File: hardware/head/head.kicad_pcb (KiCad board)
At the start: 2 copper layers, 80 x 55 mm, 50 parts, among them J1 Head bundle, J10 CM4 socket 101-200, J2 ToF, J3 I2C breakout, J4 Eye LED, J5 Speaker, J6 Fan, J7 Microphone, J8 Camera, J9 CM4 socket 1-100, Q1 AO3400A, U2 LMR51635XDDCR, U3 AMS1117-3.3, U4 MAX98357AETE+T, U5 BMI088 module

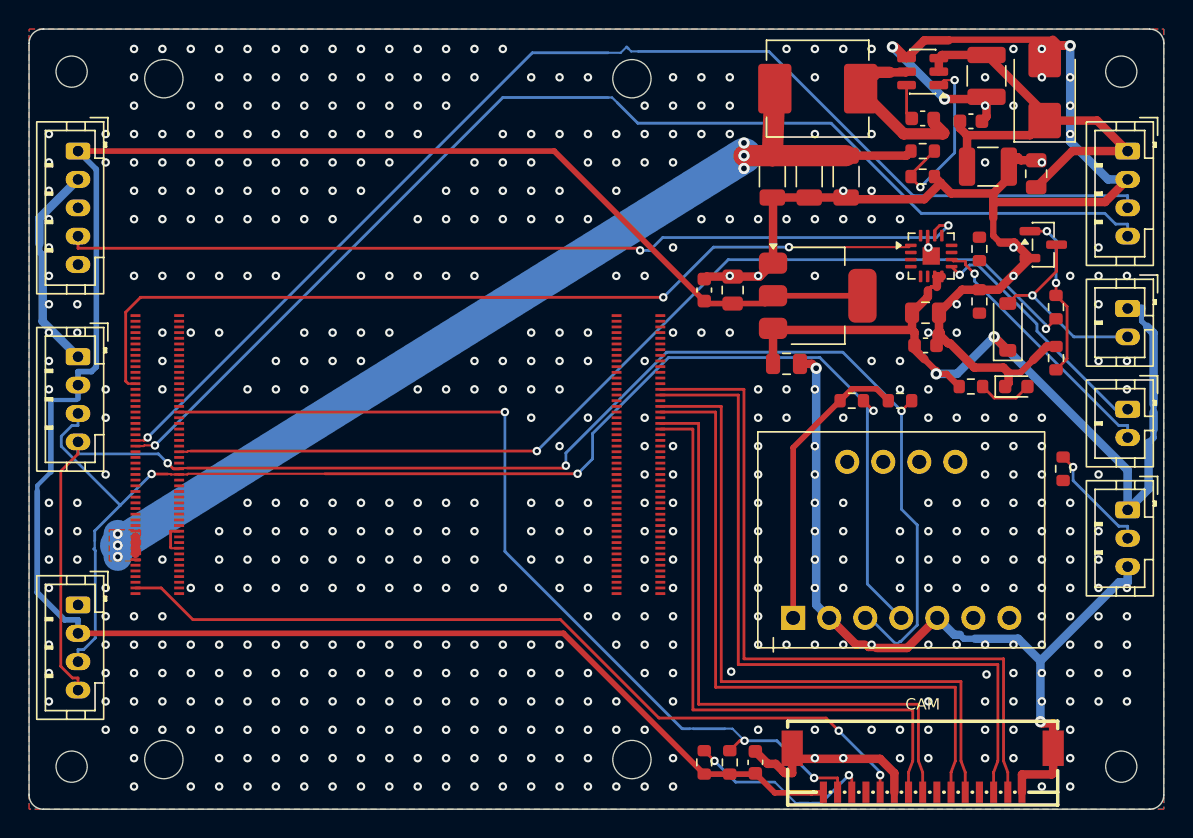
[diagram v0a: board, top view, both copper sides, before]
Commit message: Head carrier PCB: module turned 180 degrees, routing round two
J9 now faces the free block, so 5 V and most signals leave the socket
straight towards their parts; only the camera pairs cross the module,
drawn as offset polylines down the left strip and under its lower edge.
Eye LED and ToF headers in the left strip, microphone on the right.
12 connections still open, all where J9's outer row meets the 5 V run
and the AMS1117; see docs/head-pcb.md 9.1.
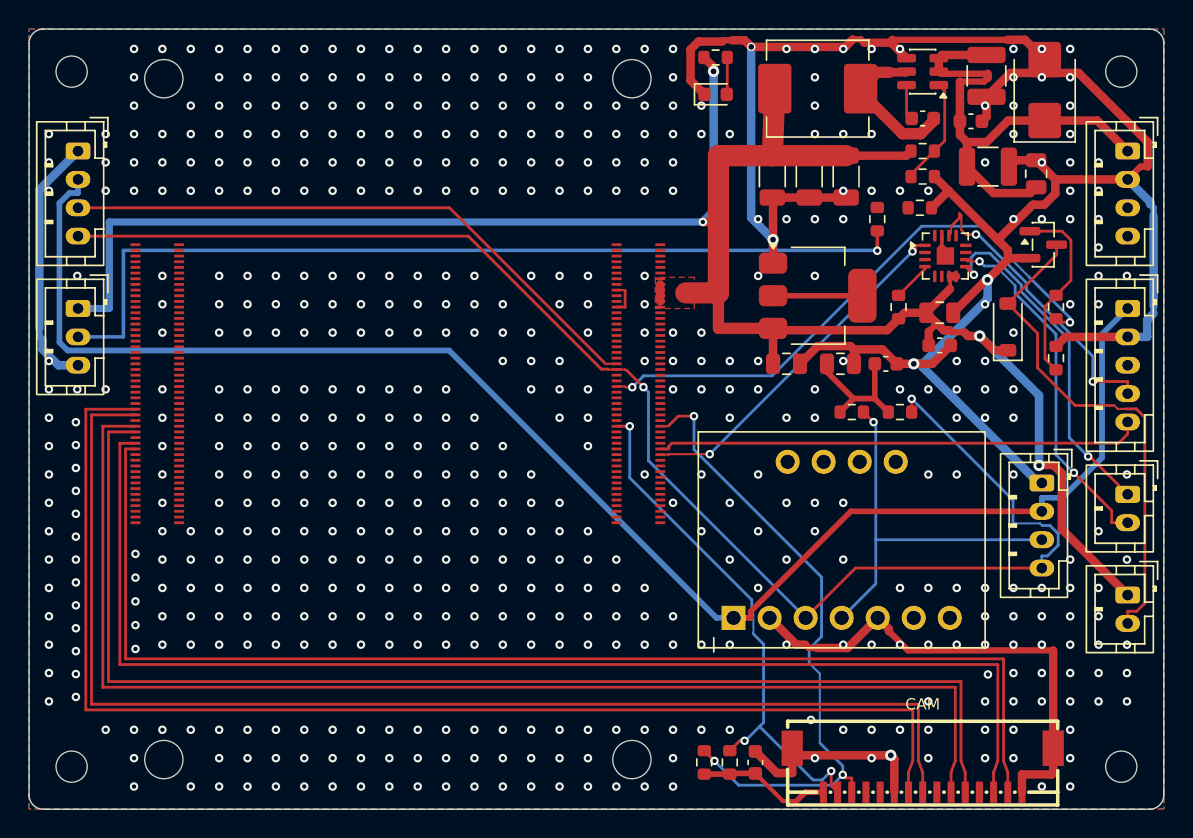
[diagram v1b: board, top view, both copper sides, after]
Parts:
- moved J4 75.4 mm to (103.5, 69.7)
- moved J7 74.8 mm to (177.4, 69.7)
- moved J3 68.5 mm to (171.4, 82.0)
- moved J10 34.3 mm to (109.0, 75.0), turned to 180 degrees
- moved J9 34.3 mm to (143.0, 75.0), turned to 180 degrees
- moved D3 29.6 mm to (148.4, 54.6)
- moved R12 29.4 mm to (148.4, 52.0)
- moved R7 21.9 mm to (159.8, 63.4), turned to -90 degrees
- moved J6 20.2 mm to (177.4, 89.9)
- moved J2 14.5 mm to (103.5, 58.6)
- moved C11 13.8 mm to (160.4, 73.6), turned to 0 degrees
- moved C10 9.21 mm to (157.2, 73.6), turned to 0 degrees
- moved R4 7.82 mm to (162.8, 62.6), turned to 0 degrees
- moved R3 7.02 mm to (161.3, 69.6)
- moved J5 6.00 mm to (177.4, 82.8)
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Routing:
- net /UART7_RX: track 86.6 -> 0.00 mm, vias 1 -> 0
- net /UART7_TX: track 84.7 -> 0.00 mm, vias 1 -> 0
- net /CAM_GPIO: track 59.3 -> 0.00 mm, vias 2 -> 0
- net /EYE_DIN: track 7.98 -> 63.9 mm
- net /CSI_C_P: track 43.5 -> 88.9 mm
- net /CSI_C_N: track 44.3 -> 88.1 mm
- net /SAI2_LRCK: track 64.5 -> 21.4 mm
- net +3V3: track 177.6 -> 136.3 mm
- net /CSI_D1_P: track 47.7 -> 88.3 mm
- net /CSI_D1_N: track 48.5 -> 87.5 mm
- net /SAI2_SDO: track 62.9 -> 24.9 mm
- net /CSI_D0_P: track 51.9 -> 87.7 mm
- net /SAI2_SDI: track 0.00 -> 34.3 mm
- net /CSI_D0_N: track 52.7 -> 86.9 mm
- net GND: track 196.3 -> 229.9 mm, vias 549 -> 576
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
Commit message: Head carrier PCB: routed, DRC clean, JLC package
UART7 and the SAI2 bit clock drawn by hand on the bottom layer from vias
beside J9; a finishing Freerouting pass (scripts/kicad/finish_head_pcb.py)
routes the rest at 0.13 mm signal clearance. DRC with schematic parity
is clean. export_jlc.py now takes the board name; the head's Gerbers,
BOM and CPL are in hardware/head/fab, with 3D renders beside the board.
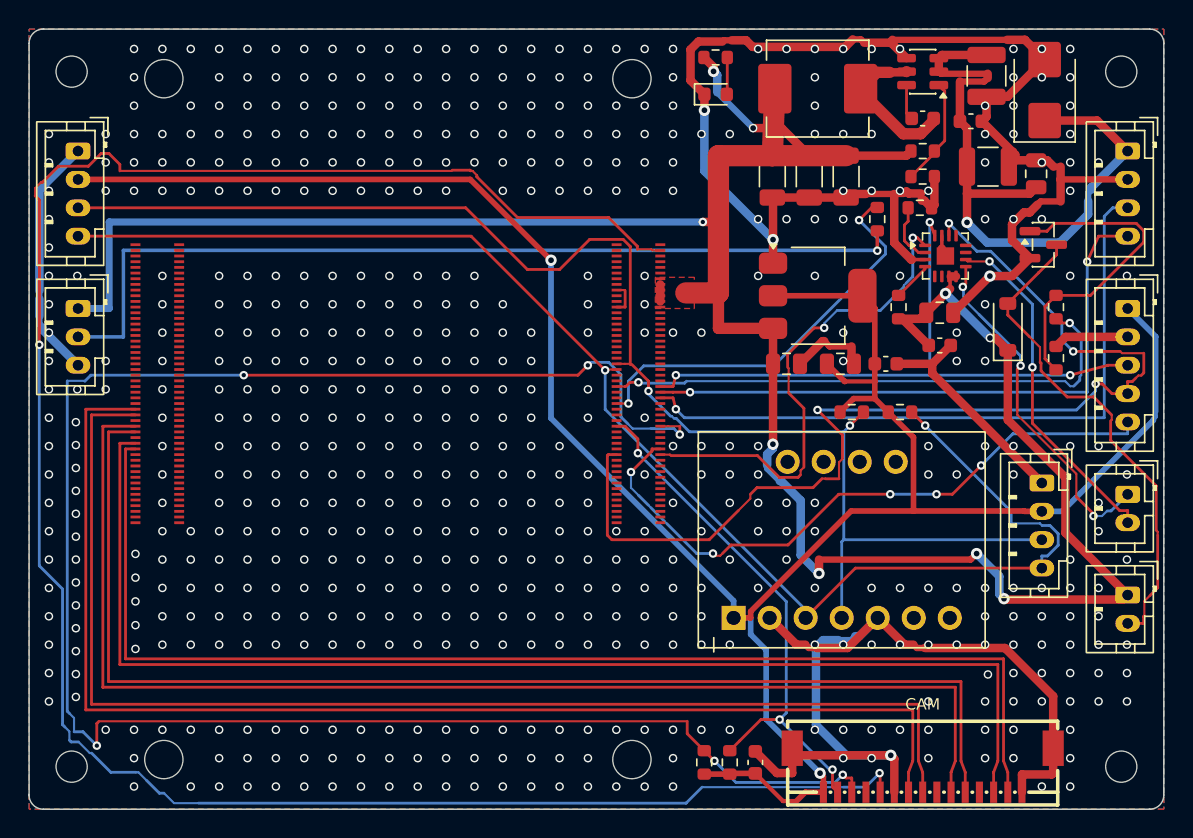
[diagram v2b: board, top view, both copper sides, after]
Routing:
- net /CAM_GPIO: track 0.00 -> 149.5 mm, vias 0 -> 2
- net /CAM_SCL: track 45.8 -> 135.0 mm, vias 3 -> 6
- net /SAI2_LRCK: track 21.4 -> 76.4 mm, vias 2 -> 4
- net /UART7_RX: track 0.00 -> 48.3 mm, vias 0 -> 1
- net /SAI2_SCLK: track 0.00 -> 45.5 mm, vias 0 -> 3
- net /UART7_TX: track 0.00 -> 43.3 mm, vias 0 -> 2
- net +5V: track 153.5 -> 182.6 mm, vias 4 -> 9
- net +3V3: track 136.3 -> 165.5 mm, vias 0 -> 2
- net /EYE_DATA: track 0.00 -> 29.1 mm, vias 0 -> 2
- net /I2C8_SDA: track 70.1 -> 97.8 mm, vias 1 -> 2
- net GND: track 229.9 -> 215.3 mm, vias 576 -> 591
- net /VBAT_IN: track 35.1 -> 47.8 mm, vias 0 -> 1
- net /SAI2_SDI: track 34.3 -> 45.3 mm, vias 0 -> 5
- net /SAI2_SDO: track 24.9 -> 34.9 mm
- net /FAN_G: track 13.4 -> 22.9 mm
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
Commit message: Head carrier PCB: BMI088 on board, fallbacks, 1.1 MHz buck (one connection open)
BMI088 chip in place of the module, with links to cut for an external
module on J3; a wide 3 A link (JP1) between the buck and the 5 V rail
with external 5 V pads (J12); a link (JP3) in the amplifier's 5 V with
module pads (J11). Buck now LMR51635YDDCR with a 4.7 uH SWPA6045.
Silkscreen labels and the name block on the back. ToF and eye headers
moved 0.3 mm clear of the module's edge. One I2C SCL connection still
open; fab outputs not regenerated. See docs/head-pcb.md 9.3.
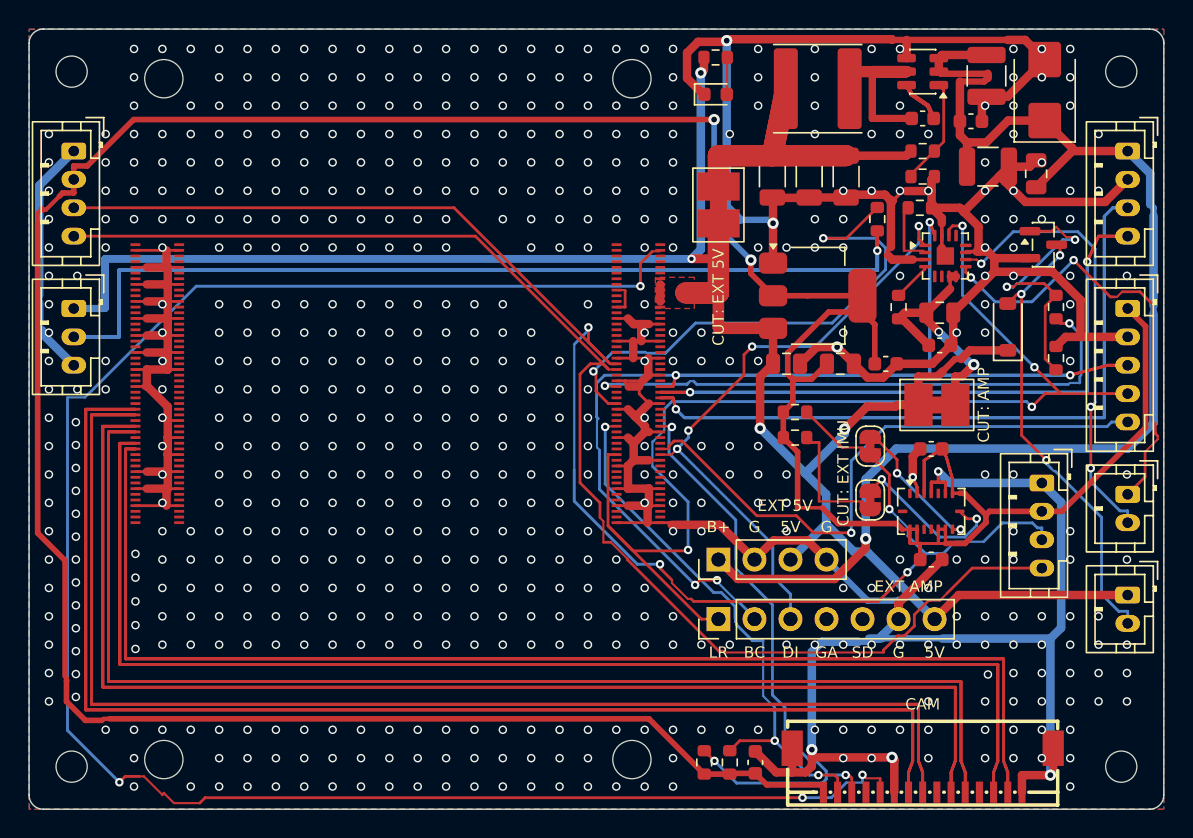
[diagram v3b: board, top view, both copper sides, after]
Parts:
- added C15: 100n 50V, Capacitor_SMD:C_0603_1608Metric, F.Cu at (163.6, 79.6)
- added C16: 100n 50V, Capacitor_SMD:C_0603_1608Metric, F.Cu at (163.6, 87.4)
- added J11: Ext amp, Connector_PinHeader_2.54mm:PinHeader_1x07_P2.54mm_Vertical, F.Cu at (148.6, 91.6)
- added J12: Ext 5V, Connector_PinHeader_2.54mm:PinHeader_1x04_P2.54mm_Vertical, F.Cu at (148.6, 87.4)
- added JP1: cut for ext 5V, DukkiHead:SolderJumper-2_Wide_Bridged_3A, F.Cu at (148.6, 62.4)
- added JP3: cut for ext amp, DukkiHead:SolderJumper-2_Wide_Bridged_3A, F.Cu at (164.0, 76.5)
- added JP4: cut for ext IMU, Jumper:SolderJumper-2_P1.3mm_Bridged_RoundedPad1.0x1.5mm, F.Cu at (159.3, 79.4)
- added JP5: cut for ext IMU, Jumper:SolderJumper-2_P1.3mm_Bridged_RoundedPad1.0x1.5mm, F.Cu at (159.3, 83.2)
- L1: value 10u -> 4.7u; footprint Inductor_SMD:L_Sunlord_MWSA0603S -> Inductor_SMD:L_Sunlord_SWPA6045S
- U2: value LMR51635XDDCR -> LMR51635YDDCR
- U5: value BMI088 module -> BMI088; footprint DukkiHead:BMI088_Module -> Package_LGA:Bosch_LGA-16_4.5x3mm_P0.5mm_LayoutBorder7x1y_ClockwisePinNumbering
- moved U5 15.8 mm to (163.6, 84.0)
- moved R9 7.62 mm to (154.0, 78.8)
- moved R8 4.00 mm to (154.0, 77.0)
- moved J2 0.30 mm to (103.2, 58.6)
- moved J4 0.30 mm to (103.2, 69.7)
- turned C5 to 180 degrees
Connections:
- C12 pad 1: +5V -> /AMP_5V
- C13 pad 1: +5V -> /AMP_5V
- C6 pad 1: +5V -> /5V_BUCK
- C7 pad 1: +5V -> /5V_BUCK
- C8 pad 1: +5V -> /5V_BUCK
- L1 pad 2: +5V -> /5V_BUCK
- R1 pad 1: +5V -> /5V_BUCK
- R3 pad 1: +5V -> /AMP_5V
- U4 pad 7: +5V -> /AMP_5V
- U4 pad 8: +5V -> /AMP_5V
- U5 pad 1: +3V3 -> unconnected-(U5-INT2-Pad1)
- U5 pad 10: unconnected-(U5-INT2-Pad10) -> +3V3
- U5 pad 11: unconnected-(U5-INT1-Pad11) -> +3V3
- U5 pad 3: /I2C8_SCL -> +3V3
- U5 pad 4: /I2C8_SDA -> GND
- U5 pad 5: GND -> unconnected-(U5-~{CSB2}-Pad5)
- U5 pad 6: unconnected-(U5-csA-Pad6) -> GND
- U5 pad 7: unconnected-(U5-csG-Pad7) -> +3V3
- U5 pad 8: unconnected-(U5-INT4-Pad8) -> /IMU_SCL
- U5 pad 9: unconnected-(U5-INT3-Pad9) -> /IMU_SDA
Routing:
- net GND: track 215.3 -> 377.8 mm, vias 591 -> 618
- net +3V3: track 165.5 -> 258.9 mm
- net /CAM_SCL: track 135.0 -> 43.2 mm, vias 6 -> 3
- net /CSI_C_P: track 88.9 -> 177.7 mm
- net /CSI_D1_P: track 88.3 -> 176.5 mm
- net /CSI_C_N: track 88.1 -> 176.1 mm
- net /CSI_D0_P: track 87.7 -> 175.3 mm
- net /CSI_D1_N: track 87.5 -> 174.9 mm
- net /CSI_D0_N: track 86.9 -> 173.7 mm
- net /SAI2_SCLK: track 45.5 -> 119.5 mm, vias 3 -> 5
- net /EYE_DIN: track 63.9 -> 128.3 mm
- net /UART7_RX: track 48.3 -> 96.5 mm
- net /VBAT_IN: track 47.8 -> 91.6 mm
- net /UART7_TX: track 43.3 -> 86.6 mm
- net /5V_BUCK: track 0.00 -> 39.3 mm
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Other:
- board text added: "5V"
- board text added: "B+"
- board text added: "BC"
- board text added: "CUT: AMP"
- board text added: "CUT: EXT 5V"
- board text added: "CUT: EXT IMU"
- board text added: "DI"
- board text added: "Dukki head"
- board text added: "EXT 5V"
- board text added: "EXT AMP"
- board text added: "G"
- board text added: "GA"
- board text added: "I2C/IMU"
- board text added: "LR"
- board text added: "SD"
- board text added: "rev A 2026"
- board text removed: "Dukki head rev A 2026"
- board text removed: "I2C"

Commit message: Head carrier PCB: last connection routed, DRC clean, JLC package regenerated
The I2C8 SCL pull-up and JP5's bus side, stranded by Freerouting, are
joined by scripts/kicad/route_one_net.py, a small two-layer maze router
for a single net. DRC with schematic parity: 0 violations, 0
unconnected. Gerbers, BOM (26 lines) and CPL (39 placements)
regenerated, with renders and the schematic PDF; about AUD 159 for 5
assembled boards before bare boards and shipping.
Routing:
- net /I2C8_SCL: track 103.3 -> 122.3 mm, vias 0 -> 6
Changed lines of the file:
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@@
+	)
+	(segment
+		(start 147.7 86)
+		(end 147.5 86)
+		(width 0.2)
+		(locked yes)
+		(layer "F.Cu")
+		(net "/I2C8_SCL")
 	)
 	(segment
@@
 	)
 	(segment
+		(start 152.7 85)
+		(end 149.6 85)
+		(width 0.2)
+		(locked yes)
+		(layer "F.Cu")
+		(net "/I2C8_SCL")
+	)
+	(segment
 		(start 162.411 91.2913)
 		(end 162.411 92.0801)
@@
 	)
 	(segment
+		(start 148.1 85.8)
+		(end 147.9 85.8)
+		(width 0.2)
+		(locked yes)
+		(layer "F.Cu")
+		(net "/I2C8_SCL")
+	)
+	(segment
 		(start 140.249 83.3983)
 		(end 138.84 81.9893)
@@
 	)
 	(segment
+		(start 149.6 85)
+		(end 148.9 84.3)
+		(width 0.2)
+		(locked yes)
+		(layer "F.Cu")
+		(net "/I2C8_SCL")
+	)
+	(segment
+		(start 155.6 83.1)
+		(end 154.9 83.1)
+		(width 0.2)
+		(locked yes)
+		(layer "F.Cu")
+		(net "/I2C8_SCL")
+	)
+	(segment
 		(start 140.249 84.4544)
 		(end 140.249 83.3983)
@@
 	)
 	(segment
+		(start 142.8 86.1)
+		(end 142.1 85.4)
+		(width 0.2)
+		(locked yes)
+		(layer "F.Cu")
+		(net "/I2C8_SCL")
+	)
+	(segment
 		(start 149.103 93.9502)
 		(end 149.015 93.8622)
@@
 	)
 	(segment
+		(start 148.9 84.3)
+		(end 148.6 84.3)
+		(width 0.2)
+		(locked yes)
+		(layer "F.Cu")
+		(net "/I2C8_SCL")
+	)
+	(segment
 		(start 161.245 92.775)
 		(end 160.235 93.785)
@@
 	)
 	(segment
+		(start 147.9 85.8)
+		(end 147.7 86)
+		(width 0.2)
+		(locked yes)
+		(layer "F.Cu")
+		(net "/I2C8_SCL")
+	)
+	(segment
+		(start 147.5 86)
+		(end 147.4 86.1)
+		(width 0.2)
+		(locked yes)
+		(layer "F.Cu")
+		(net "/I2C8_SCL")
+	)
+	(segment
 		(start 142.186 87.4052)
 		(end 142.183 87.4052)
@@
 	)
 	(segment
+		(start 148.6 84.3)
+		(end 148.4 84.1)
+		(width 0.2)
+		(locked yes)
+		(layer "F.Cu")
+		(net "/I2C8_SCL")
+	)
+	(segment
+		(start 147.4 86.1)
+		(end 142.8 86.1)
+		(width 0.2)
+		(locked yes)
+		(layer "F.Cu")
+		(net "/I2C8_SCL")
+	)
+	(segment
 		(start 140.818 73.9502)
 		(end 140.843 73.9754)
@@
 		(net "/I2C8_SCL")
 	)
+	(via
+		(at 148.1 85.8)
+		(size 0.6)
+		(drill 0.3)
+		(layers "F.Cu" "B.Cu")
+		(locked yes)
+		(net "/I2C8_SCL")
+	)
+	(via
+		(at 152.7 85)
+		(size 0.6)
+		(drill 0.3)
+		(layers "F.Cu" "B.Cu")
+		(locked yes)
+		(net "/I2C8_SCL")
+	)
+	(via
+		(at 142.1 85.4)
+		(size 0.6)
+		(drill 0.3)
+		(layers "F.Cu" "B.Cu")
+		(locked yes)
+		(net "/I2C8_SCL")
+	)
+	(via
+		(at 154.9 83.1)
+		(size 0.6)
+		(drill 0.3)
+		(layers "F.Cu" "B.Cu")
+		(locked yes)
+		(net "/I2C8_SCL")
+	)
+	(via
+		(at 148.4 84.1)
+		(size 0.6)
+		(drill 0.3)
+		(layers "F.Cu" "B.Cu")
+		(locked yes)
+		(net "/I2C8_SCL")
+	)
+	(via
+		(at 140.2 84.2)
+		(size 0.6)
+		(drill 0.3)
+		(layers "F.Cu" "B.Cu")
+		(locked yes)
+		(net "/I2C8_SCL")
+	)
+	(segment
+		(start 148.4 85.5)
+		(end 148.1 85.8)
+		(width 0.2)
+		(locked yes)
+		(layer "B.Cu")
+		(net "/I2C8_SCL")
+	)
+	(segment
+		(start 148.4 84.1)
+		(end 148.4 85.5)
+		(width 0.2)
+		(locked yes)
+		(layer "B.Cu")
+		(net "/I2C8_SCL")
+	)
+	(segment
+		(start 154.9 83.1)
+		(end 154.6 83.1)
+		(width 0.2)
+		(locked yes)
+		(layer "B.Cu")
+		(net "/I2C8_SCL")
+	)
+	(segment
+		(start 141.4 85.4)
+		(end 140.2 84.2)
+		(width 0.2)
+		(locked yes)
+		(layer "B.Cu")
+		(net "/I2C8_SCL")
+	)
+	(segment
+		(start 154.6 83.1)
+		(end 152.7 85)
+		(width 0.2)
+		(locked yes)
+		(layer "B.Cu")
+		(net "/I2C8_SCL")
+	)
+	(segment
+		(start 142.1 85.4)
+		(end 141.4 85.4)
+		(width 0.2)
+		(locked yes)
+		(layer "B.Cu")
+		(net "/I2C8_SCL")
+	)
